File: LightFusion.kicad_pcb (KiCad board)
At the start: 2 copper layers, 52 x 52 mm, 78 parts, among them IC1 MCP3561T-E_ST, IC2 ADS1291IPBSR, J1 303C-C4115-30-04, P1 PHR-2, U1 BMD-350-A-R, U2 TPS7A2033PDBVR, U3 TPS22918DBVR

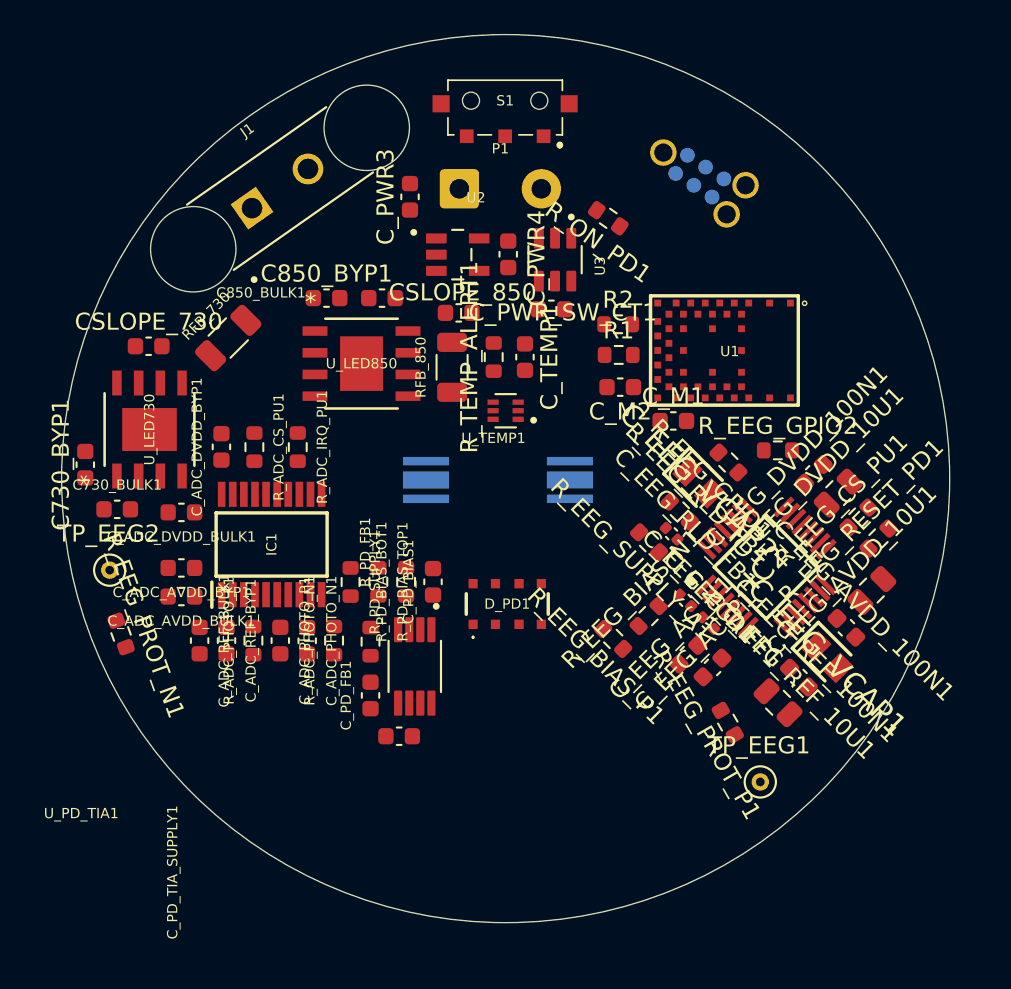
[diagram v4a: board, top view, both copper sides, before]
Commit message: eeg 3rd electrode added
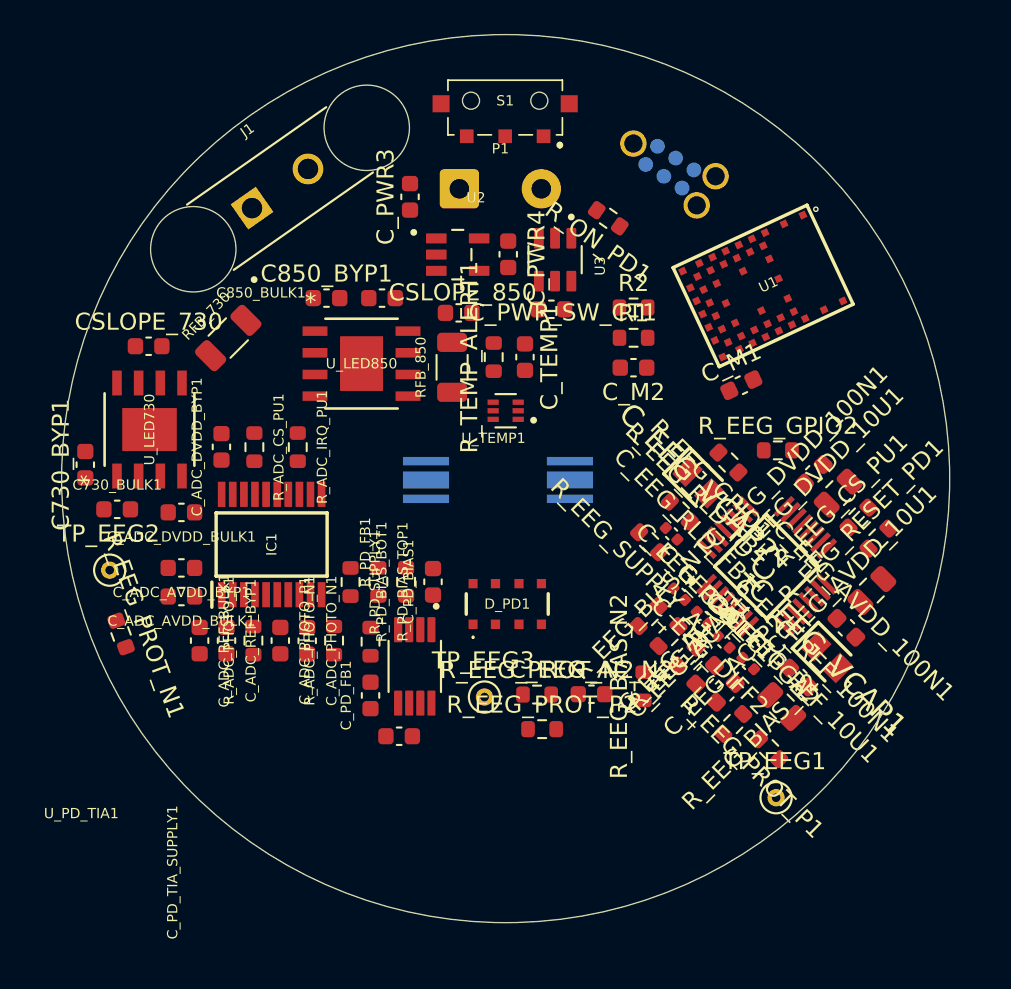
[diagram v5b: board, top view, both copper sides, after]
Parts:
- added C_EEG_AC_N2: 47 nF, LightFusion:C_0603_1608Metric, F.Cu at (155.0, 142.6)
- added C_EEG_AC_P2: 47 nF, LightFusion:C_0603_1608Metric, F.Cu at (162.9, 142.5)
- added C_EEG_DIFF2: 2.2 nF, LightFusion:C_0402_1005Metric, F.Cu at (162.8, 139.6)
- added C_EEG_PGA2: 4.7 nF, LightFusion:C_0402_1005Metric, F.Cu at (164.2, 140.8)
- added R_EEG_BIAS_N2: 22 MΩ, LightFusion:R_0603_1608Metric, F.Cu at (158.1, 142.2)
- added R_EEG_BIAS_P2: 22 MΩ, LightFusion:R_0603_1608Metric, F.Cu at (163.3, 144.4)
- added R_EEG_PROT_N2: 51 kΩ, LightFusion:R_0603_1608Metric, F.Cu at (151.8, 142.6)
- added R_EEG_PROT_P2: 51 kΩ, LightFusion:R_0603_1608Metric, F.Cu at (152.1, 144.7)
- added TP_EEG3: TestPoint, LightFusion:MILL-MAX_0906-0-15-20-76-14-11-0, F.Cu at (148.8, 142.8)
- IC2: value ADS1291IPBSR -> ADS1292IPBSR; footprint LightFusion:ADS1291IPBSR -> LightFusion:ADS1292IPBSR
- moved C_M1 4.50 mm to (163.8, 124.5), turned to 25 degrees
- moved U1 4.41 mm to (165.1, 118.7), turned to -155 degrees
- moved R_EEG_BIAS_P1 3.24 mm to (159.5, 139.2), turned to -135 degrees
- moved R_EEG_PROT_P1 2.88 mm to (165.4, 145.8), turned to 135 degrees
- moved J_PROG1 1.83 mm to (159.6, 111.8)
- moved C_M2 1.38 mm to (157.5, 123.5)
- moved R2 1.34 mm to (157.5, 120.0)
- moved R1 1.33 mm to (157.5, 121.8)
- moved TP_EEG1 1.31 mm to (165.8, 148.7)
- moved C_EEG_AC_P1 0.61 mm to (161.7, 141.5)
- moved C_EEG_PGA1 0.51 mm to (160.2, 136.8)
- moved C_EEG_DIFF1 0.47 mm to (161.5, 138.1)
- moved C_EEG_REF_10U1 0.31 mm to (166.2, 143.3)
- moved C_EEG_AC_N1 0.14 mm to (160.6, 140.4)
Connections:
- IC2 pad 31: /3V3_EEG_A -> unconnected-(IC2-RESP_MODP/IN3P-Pad31)
- IC2 pad 5: /3V3_EEG_A -> Net-(IC2-IN2N)
- IC2 pad 6: /3V3_EEG_A -> Net-(IC2-IN2P)
- IC2 pad 7: unconnected-(IC2-PGA2N-Pad7) -> Net-(IC2-PGA2N)
- IC2 pad 8: unconnected-(IC2-PGA2P-Pad8) -> Net-(IC2-PGA2P)

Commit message: remove silk screen removed from pcb
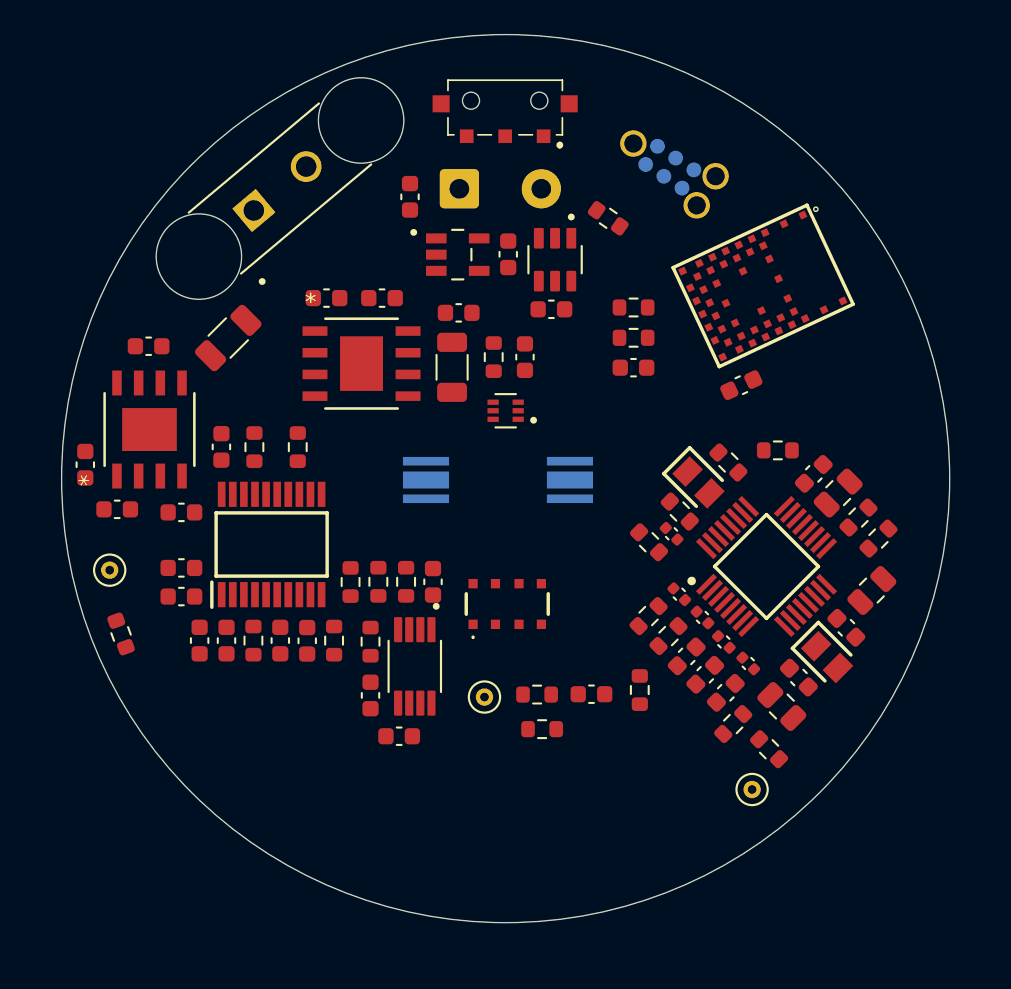
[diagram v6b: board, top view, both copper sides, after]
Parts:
- moved TP_EEG1 1.48 mm to (164.4, 148.2)
- moved R_EEG_BIAS_N2 0.30 mm to (157.9, 142.4)
- turned J1 to 40 degrees
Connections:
- IC2 pad 31: unconnected-(IC2-RESP_MODP/IN3P-Pad31) -> /3V3_EEG_A

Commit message: 2 layers without GND and PWM PWR yet pcb
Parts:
- moved R_EEG_GPIO2 1.78 mm to (164.2, 127.9), turned to 135 degrees
- moved C_EEG_DVDD_10U1 1.53 mm to (168.4, 129.8)
- moved C_EEG_DVDD_100N1 1.51 mm to (167.0, 128.7)
- moved R_ADC_IRQ_PU1 0.98 mm to (138.8, 128.2)
- moved R_EEG_BIAS_N2 0.35 mm to (157.5, 142.4)
- moved R_ADC_CS_PU1 0.31 mm to (135.0, 128.2)
- moved R_EEG_SUPPLY_A1 0.17 mm to (158.3, 133.9)
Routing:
- net 3V3_DIG: track 0.00 -> 60.0 mm
- net Net-(C_EEG_AC_N1-Pad1): track 0.00 -> 52.5 mm, vias 0 -> 2
- net VBAT_SYSTEM: track 0.00 -> 36.4 mm
- net /PD_ADC/3V3_A: track 0.00 -> 30.9 mm
- net ADC_SCK: track 0.00 -> 27.3 mm, vias 0 -> 3
- net /EEG_BIAS: track 0.00 -> 25.5 mm
- net ADC_MOSI: track 0.00 -> 25.1 mm, vias 0 -> 3
- net ADC_MISO: track 0.00 -> 22.9 mm, vias 0 -> 3
- net /EEG_DRDY: track 0.00 -> 22.4 mm, vias 0 -> 2
- net /Power/BAT+: track 0.00 -> 19.5 mm
- net I2C_TEMP_SDA: track 0.00 -> 17.2 mm, vias 0 -> 2
- net /PD_ADC/PHOTO_OUT: track 0.00 -> 15.8 mm
- net /3V3_EEG_A: track 0.00 -> 10.1 mm
- net Net-(C_EEG_AC_P2-Pad1): track 0.00 -> 10.0 mm
- net /PD_ADC/PHOTO_BIAS: track 0.00 -> 9.79 mm
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
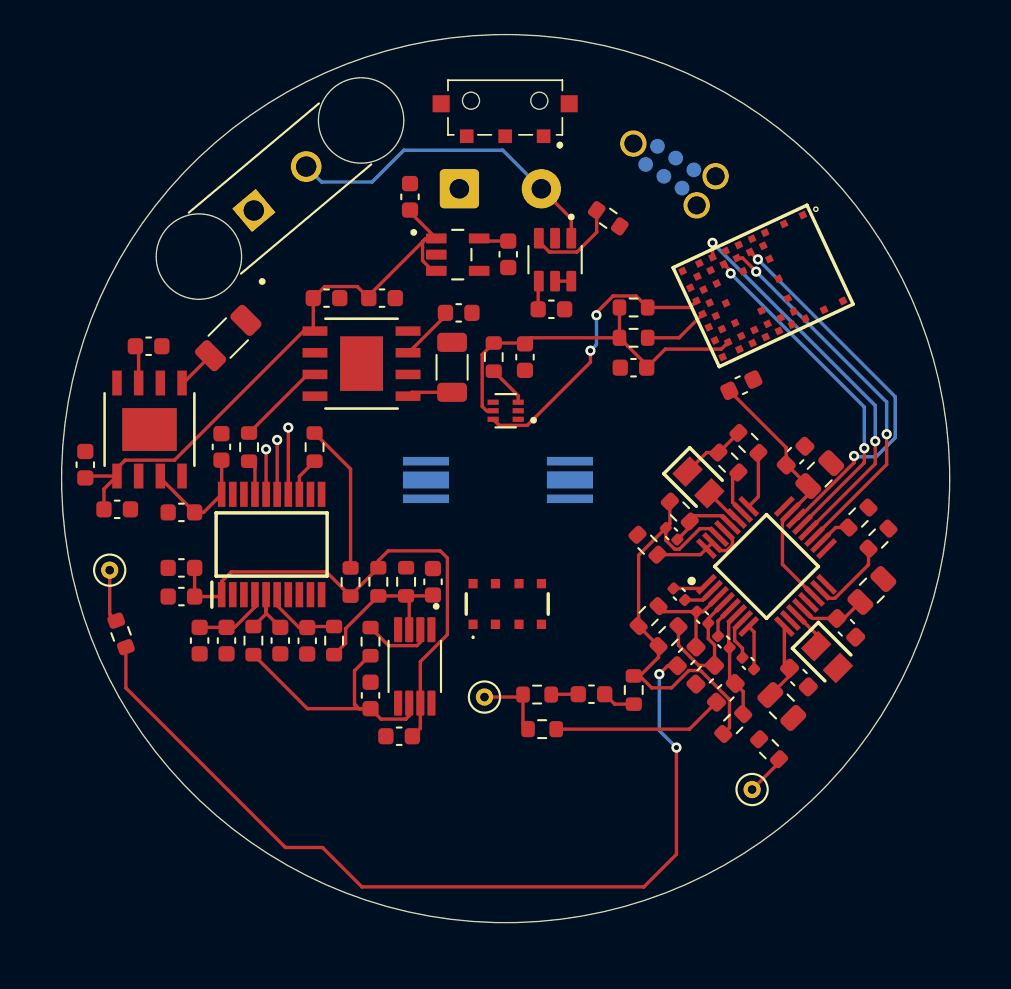
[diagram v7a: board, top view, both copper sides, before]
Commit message: 4 layers without GND not ready
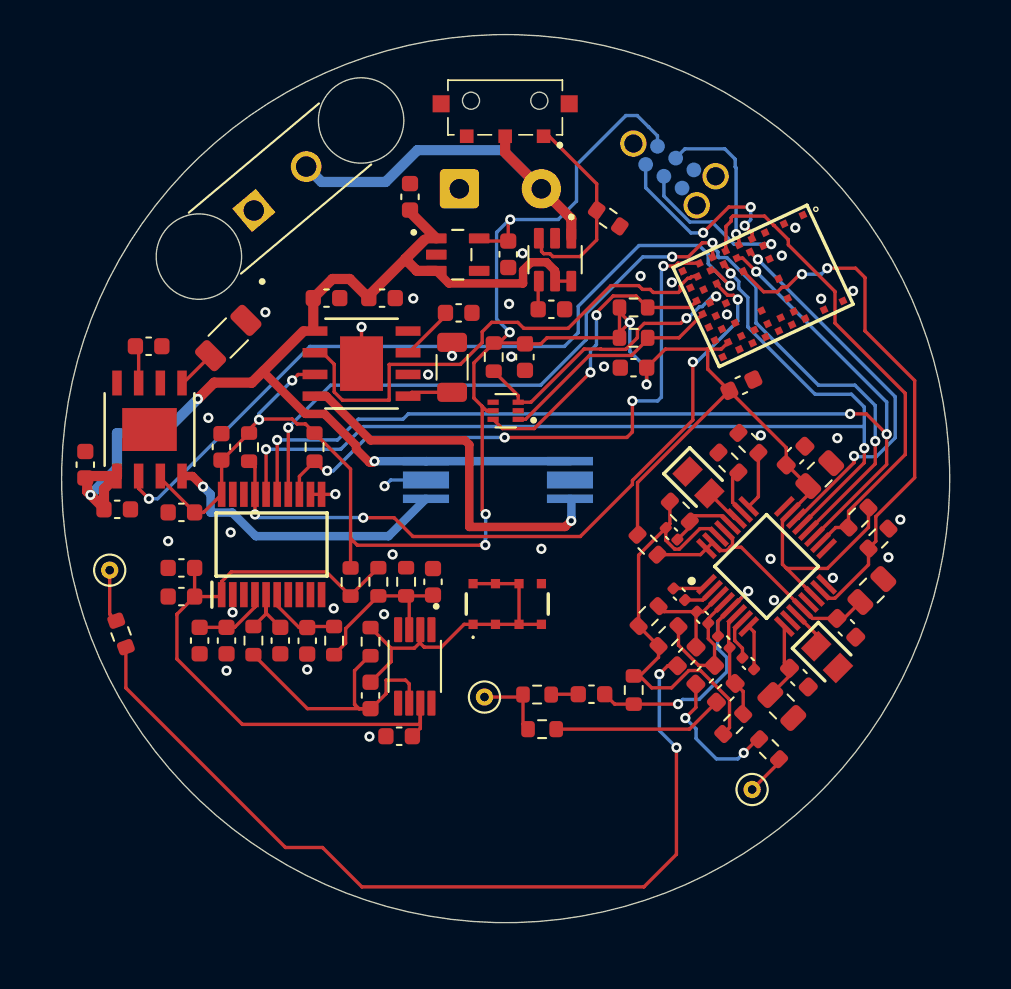
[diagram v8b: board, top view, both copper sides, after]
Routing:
- net GND: track 3.91 -> 344.1 mm, vias 0 -> 36
- net 3V3_DIG: track 60.0 -> 132.5 mm, vias 0 -> 8
- net PWM_730: track 0.00 -> 45.5 mm, vias 0 -> 2
- net ADC_DRDY_N: track 2.08 -> 42.3 mm, vias 0 -> 4
- net VBAT_SYSTEM: track 36.4 -> 73.3 mm, vias 0 -> 3
- net ADC_MISO: track 22.9 -> 59.7 mm
- net ADC_MOSI: track 25.1 -> 61.9 mm, vias 3 -> 4
- net ADC_CS_N: track 2.31 -> 35.6 mm, vias 0 -> 4
- net ADC_SCK: track 27.3 -> 59.0 mm, vias 3 -> 4
- net PWM_850: track 0.00 -> 29.9 mm
- net /EEG_CS_N: track 2.00 -> 29.1 mm
- net /EEG_RESET_N: track 4.76 -> 31.4 mm, vias 0 -> 2
- net /LED/LED850_K: track 0.00 -> 22.6 mm, vias 0 -> 1
- net /LED/LED730_K: track 0.00 -> 17.3 mm, vias 0 -> 1
- net /PD_ADC/PHOTO_TIA_IN: track 4.17 -> 20.4 mm
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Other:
- copper layers 2 -> 4
